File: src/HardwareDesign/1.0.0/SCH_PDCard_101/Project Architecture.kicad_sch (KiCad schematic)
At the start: 27 parts, among them J1 USB_C_Receptacle_PowerOnly_6P

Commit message: Baseboard design start
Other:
- sheet USB-PD Source Controller: file Section B - TItle B.kicad_sch -> usb_pd_source_controller.kicad_sch
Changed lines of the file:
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@@
 		)
 		(instances
-			(project "PDNode-600"
+			(project "PDNode-PDCard"
 				(path "/f9e05184-c88b-4a88-ae9c-ab2bdb32be7c/c5103ceb-5325-4a84-a025-9638a412984e"
 					(page "5")
@@
 			)
 		)
-		(property "Sheetfile" "Section B - TItle B.kicad_sch"
+		(property "Sheetfile" "usb_pd_source_controller.kicad_sch"
 			(at 262.636 224.282 0)
 			(effects
@@
 		)
 		(instances
-			(project "PDNode-600"
+			(project "PDNode-PDCard"
 				(path "/f9e05184-c88b-4a88-ae9c-ab2bdb32be7c/c5103ceb-5325-4a84-a025-9638a412984e"
 					(page "4")
@@
 		)
 		(instances
-			(project "PDNode-600"
+			(project "PDNode-PDCard"
 				(path "/f9e05184-c88b-4a88-ae9c-ab2bdb32be7c/c5103ceb-5325-4a84-a025-9638a412984e"
 					(page "3")

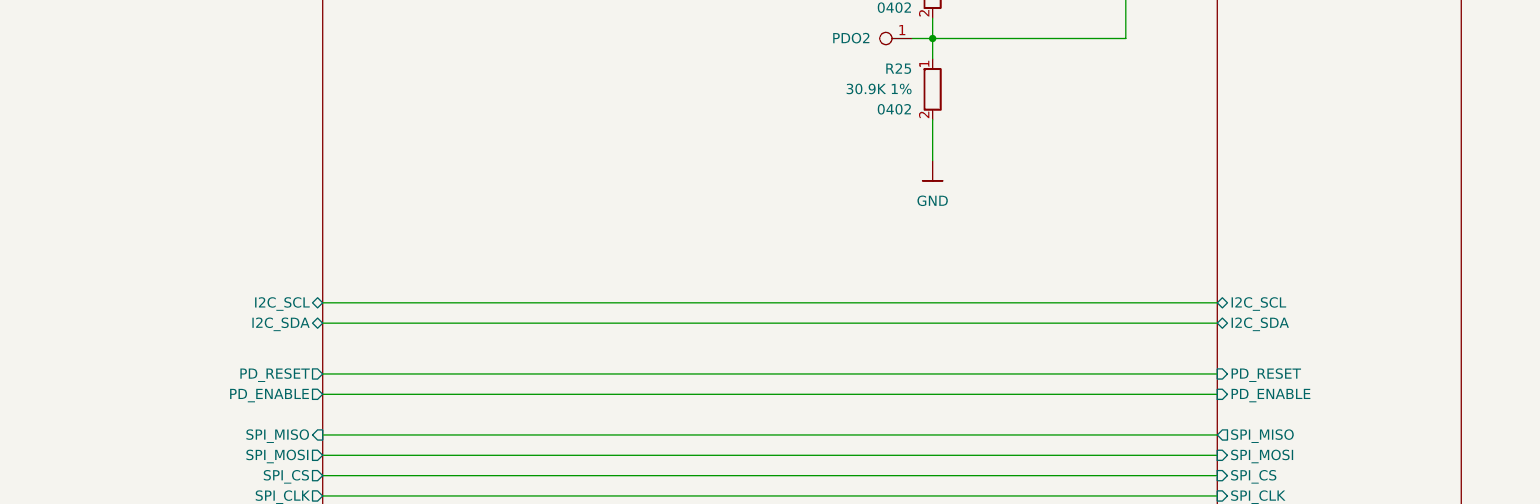
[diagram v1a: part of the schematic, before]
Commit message: Add bladecore to design
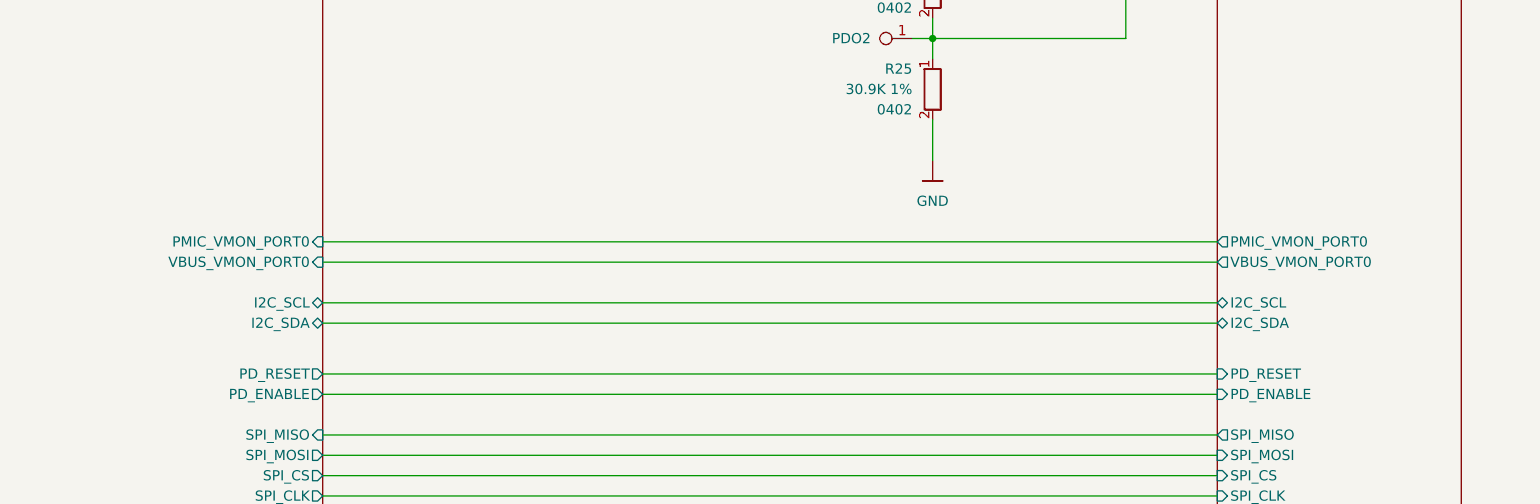
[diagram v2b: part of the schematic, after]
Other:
- sheet Board Connector and Supplies ports: added PMIC_VMON_PORT0, VBUS_VMON_PORT0; removed none
- sheet USB-PD Source Controller ports: added PMIC_VMON_PORT0, VBUS_VMON_PORT0; removed none
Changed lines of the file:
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@@
 	(wire
 		(pts
+			(xy 151.13 180.34) (xy 262.89 180.34)
+		)
+		(stroke
+			(width 0)
+			(type default)
+		)
+	)
+	(wire
+		(pts
 			(xy 227.33 95.25) (xy 227.33 101.6)
 		)
@@
 	(wire
 		(pts
+			(xy 151.13 182.88) (xy 262.89 182.88)
+		)
+		(stroke
+			(width 0)
+			(type default)
+		)
+	)
+	(wire
+		(pts
 			(xy 331.47 81.28) (xy 354.33 81.28)
 		)
@@
 			)
 		)
+		(pin "VBUS_VMON_PORT0" input
+			(at 151.13 182.88 0)
+			(effects
+				(font
+					(size 1.27 1.27)
+				)
+				(justify right)
+			)
+		)
+		(pin "PMIC_VMON_PORT0" input
+			(at 151.13 180.34 0)
+			(effects
+				(font
+					(size 1.27 1.27)
+				)
+				(justify right)
+			)
+		)
 		(instances
 			(project "PDNode-PDCard"
@@
 			(effects
 				(font
+					(size 1.27 1.27)
+				)
+				(justify left)
+			)
+		)
+		(pin "PMIC_VMON_PORT0" output
+			(at 262.89 180.34 180)
+			(effects
+				(font
+					(size 1.27 1.27)
+				)
+				(justify left)
+			)
+		)
+		(pin "VBUS_VMON_PORT0" output
+			(at 262.89 182.88 180)
+			(effects
+				(font
